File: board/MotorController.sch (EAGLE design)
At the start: 39 parts, among them IC1 ATMEGA328P-PU, Q1 BT137-600E, Q2 IPP80P03P4L-04, Q3 SUP75P03-07-H-NH, Y1 16Mhz

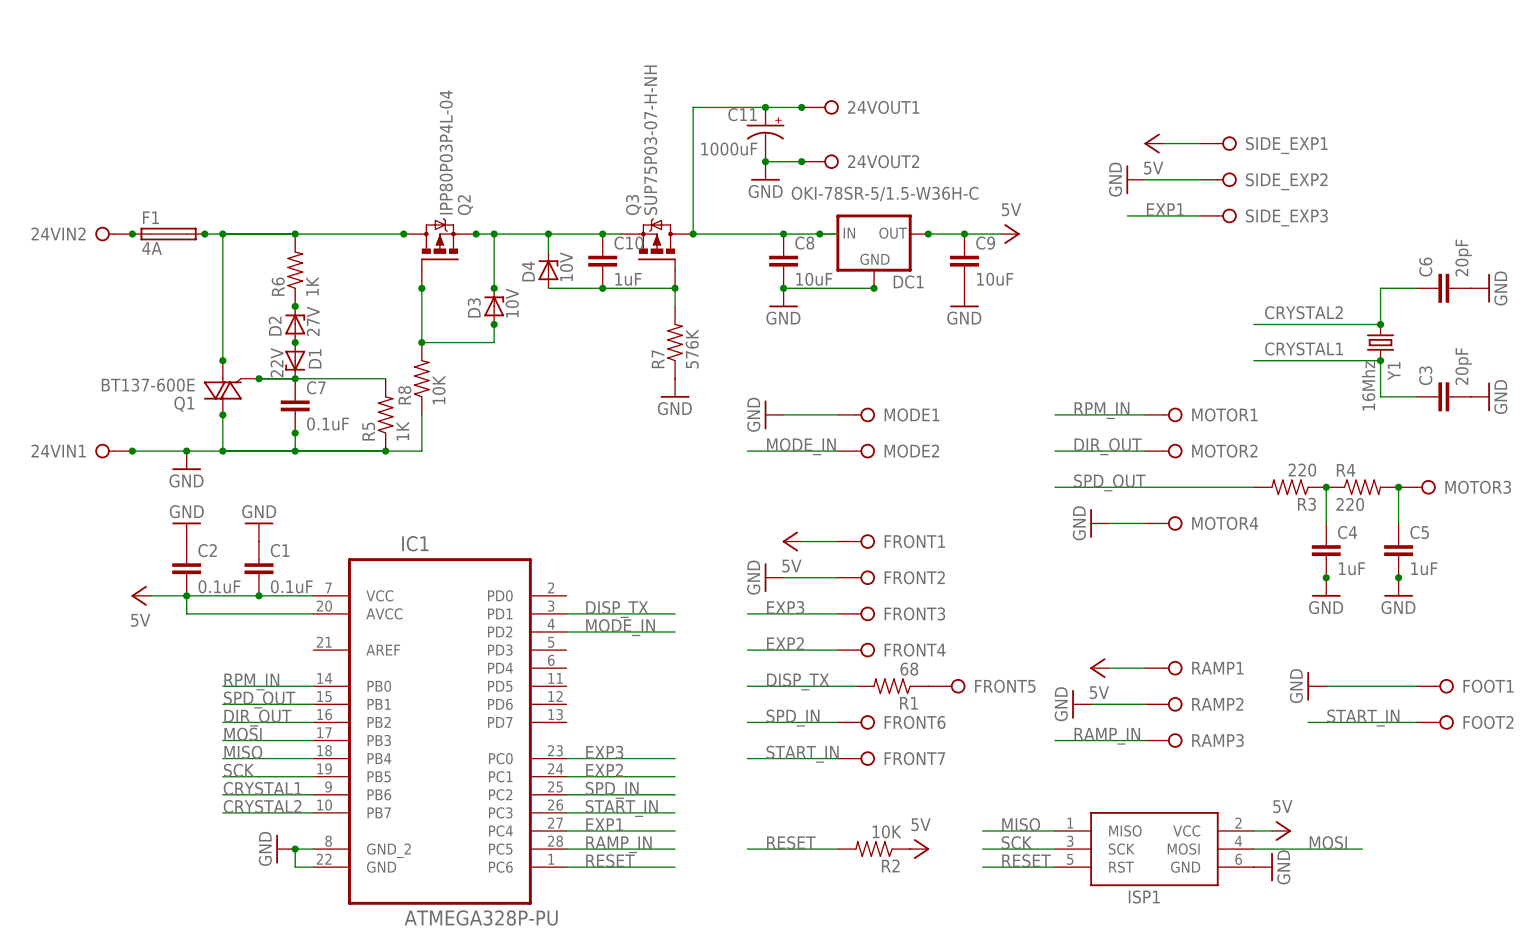
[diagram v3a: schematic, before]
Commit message: Fix the label order of caps
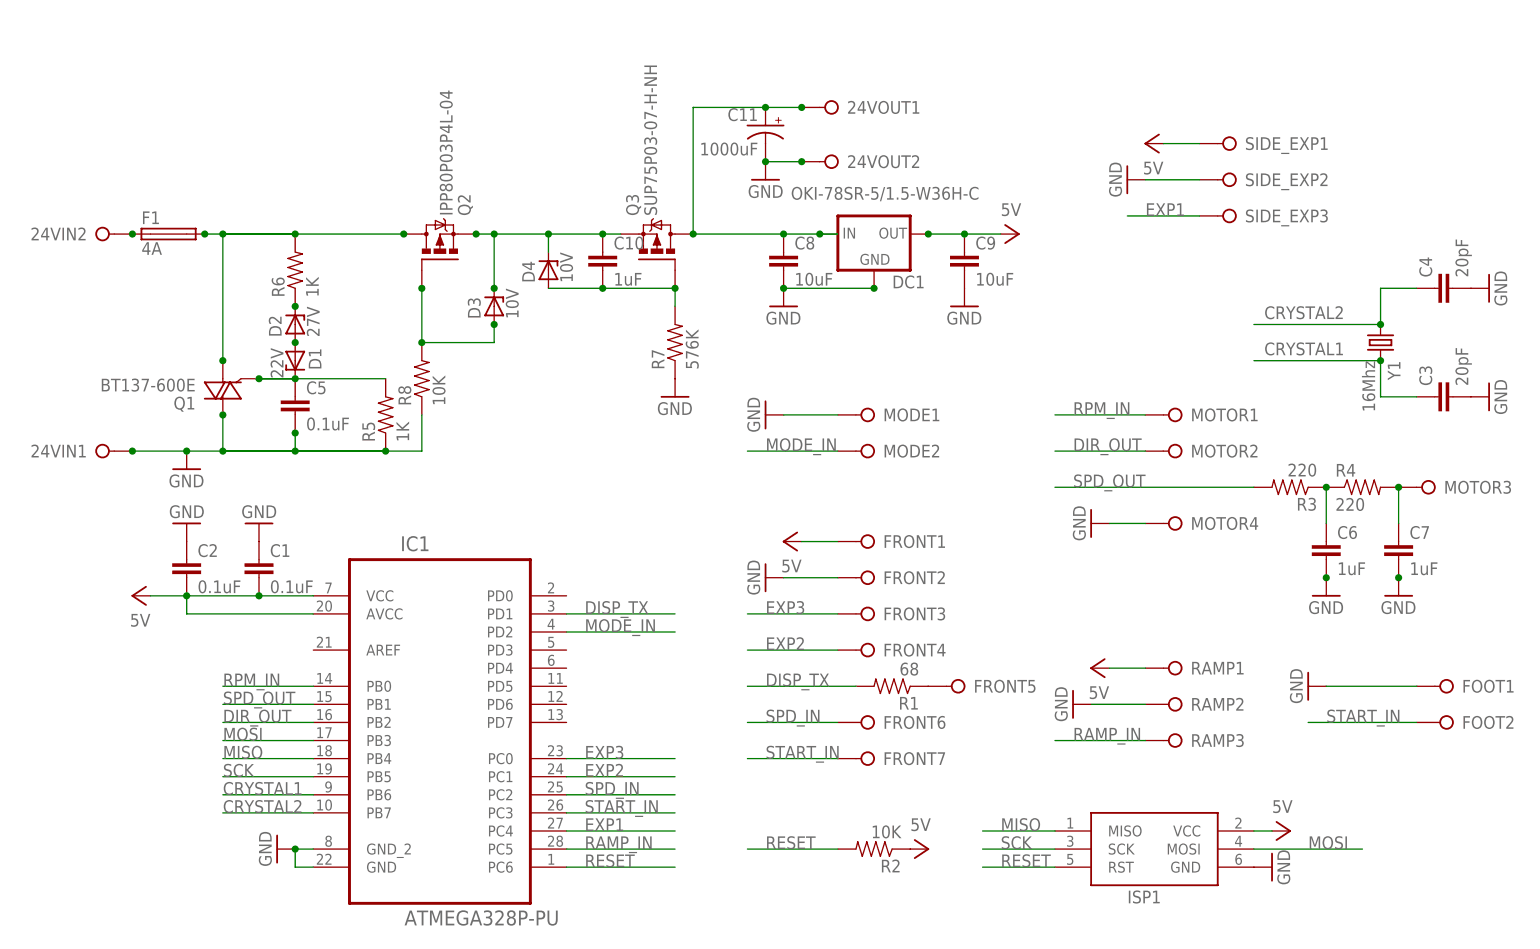
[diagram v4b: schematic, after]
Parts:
- C4: value 1uF -> 20pF
- C5: value 1uF -> 0.1uF
- C6: value 20pF -> 1uF
- C7: value 0.1uF -> 1uF
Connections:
- net CRYSTAL2: now also C4.1; no longer C6.1
- net N$1: now also C6.1; no longer C4.1
- net N$10: now also C7.1; no longer C5.1
- net N$7: now also C5.1; no longer C7.1
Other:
- moved on the sheet: C4, C5, C6, C7
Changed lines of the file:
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@@
 <part name="D2" library="SaintGimp" deviceset="ZENER" device="-7.5" value="27V"/>
 <part name="R6" library="SaintGimp" deviceset="RESISTOR-*" device="7.5MM" value="1K"/>
-<part name="C7" library="SaintGimp" deviceset="CAPACITOR-*" device="2.5MM" value="0.1uF"/>
+<part name="C5" library="SaintGimp" deviceset="CAPACITOR-*" device="2.5MM" value="0.1uF"/>
 <part name="R5" library="SaintGimp" deviceset="RESISTOR-*" device="7.5MM" value="1K"/>
 <part name="Q2" library="SaintGimp" deviceset="IPP80P03P4L-04" device="-H-NH" value="IPP80P03P4L-04"/>
@@
 <part name="R3" library="SaintGimp" deviceset="RESISTOR-*" device="7.5MM" value="220"/>
 <part name="R4" library="SaintGimp" deviceset="RESISTOR-*" device="7.5MM" value="220"/>
-<part name="C4" library="SaintGimp" deviceset="CAPACITOR-*" device="2.5MM" value="1uF"/>
+<part name="C6" library="SaintGimp" deviceset="CAPACITOR-*" device="2.5MM" value="1uF"/>
 <part name="GND7" library="SaintGimp" deviceset="GND" device=""/>
-<part name="C5" library="SaintGimp" deviceset="CAPACITOR-*" device="2.5MM" value="1uF"/>
+<part name="C7" library="SaintGimp" deviceset="CAPACITOR-*" device="2.5MM" value="1uF"/>
 <part name="GND8" library="SaintGimp" deviceset="GND" device=""/>
 <part name="Y1" library="SaintGimp" deviceset="CRYSTAL" device="-V" value="16Mhz"/>
 <part name="GND10" library="SaintGimp" deviceset="GND" device=""/>
 <part name="C3" library="SaintGimp" deviceset="CAPACITOR-*" device="2.5MM" value="20pF"/>
-<part name="C6" library="SaintGimp" deviceset="CAPACITOR-*" device="2.5MM" value="20pF"/>
+<part name="C4" library="SaintGimp" deviceset="CAPACITOR-*" device="2.5MM" value="20pF"/>
 <part name="GND11" library="SaintGimp" deviceset="GND" device=""/>
 <part name="GND12" library="SaintGimp" deviceset="GND" device=""/>
@@
 <instance part="D2" gate="G$1" x="-25.4" y="40.64" rot="R90"/>
 <instance part="R6" gate="G$1" x="-25.4" y="48.26" rot="R90"/>
-<instance part="C7" gate="G$1" x="-25.4" y="27.94"/>
+<instance part="C5" gate="G$1" x="-25.4" y="27.94"/>
 <instance part="R5" gate="G$1" x="-12.7" y="27.94" rot="R90"/>
 <instance part="Q2" gate="G$1" x="-5.08" y="50.8" rot="MR90"/>
@@
 <instance part="R3" gate="G$1" x="114.3" y="17.78" rot="R180"/>
 <instance part="R4" gate="G$1" x="124.46" y="17.78"/>
-<instance part="C4" gate="G$1" x="119.38" y="7.62"/>
+<instance part="C6" gate="G$1" x="119.38" y="7.62"/>
 <instance part="GND7" gate="1" x="119.38" y="2.54"/>
-<instance part="C5" gate="G$1" x="129.54" y="7.62"/>
+<instance part="C7" gate="G$1" x="129.54" y="7.62"/>
 <instance part="GND8" gate="1" x="129.54" y="2.54"/>
 <instance part="Y1" gate="G$1" x="127" y="38.1" rot="R270"/>
 <instance part="GND10" gate="1" x="-30.48" y="12.7" rot="R180"/>
 <instance part="C3" gate="G$1" x="137.16" y="30.48" rot="R90"/>
-<instance part="C6" gate="G$1" x="137.16" y="45.72" rot="R90"/>
+<instance part="C4" gate="G$1" x="137.16" y="45.72" rot="R90"/>
 <instance part="GND11" gate="1" x="142.24" y="30.48" rot="R90"/>
 <instance part="GND12" gate="1" x="142.24" y="45.72" rot="R90"/>
@@
 <wire x1="-12.7" y1="22.86" x2="-25.4" y2="22.86" width="0.1524" layer="91"/>
 <junction x="-12.7" y="22.86"/>
-<pinref part="C7" gate="G$1" pin="2"/>
+<pinref part="C5" gate="G$1" pin="2"/>
 <wire x1="-25.4" y1="22.86" x2="-35.56" y2="22.86" width="0.1524" layer="91"/>
 <wire x1="-35.56" y1="22.86" x2="-40.64" y2="22.86" width="0.1524" layer="91"/>
@@
 </segment>
 <segment>
-<pinref part="C5" gate="G$1" pin="2"/>
+<pinref part="C7" gate="G$1" pin="2"/>
 <pinref part="GND8" gate="1" pin="GND"/>
 <junction x="129.54" y="5.08"/>
@@
 </segment>
 <segment>
+<pinref part="C4" gate="G$1" pin="2"/>
+<pinref part="GND12" gate="1" pin="GND"/>
+</segment>
+<segment>
 <pinref part="C6" gate="G$1" pin="2"/>
-<pinref part="GND12" gate="1" pin="GND"/>
-</segment>
-<segment>
-<pinref part="C4" gate="G$1" pin="2"/>
-<pinref part="C4" gate="G$1" pin="2"/>
+<pinref part="C6" gate="G$1" pin="2"/>
 <pinref part="GND7" gate="1" pin="GND"/>
 <junction x="119.38" y="5.08"/>
@@
 <pinref part="D1" gate="G$1" pin="C"/>
 <wire x1="-30.48" y1="33.02" x2="-25.4" y2="33.02" width="0.1524" layer="91"/>
-<pinref part="C7" gate="G$1" pin="1"/>
+<pinref part="C5" gate="G$1" pin="1"/>
 <junction x="-25.4" y="33.02"/>
 <pinref part="R5" gate="G$1" pin="2"/>
@@
 <segment>
 <pinref part="R4" gate="G$1" pin="2"/>
-<pinref part="C5" gate="G$1" pin="1"/>
+<pinref part="C7" gate="G$1" pin="1"/>
 <wire x1="129.54" y1="12.7" x2="129.54" y2="17.78" width="0.1524" layer="91"/>
 <pinref part="MOTOR" gate="3" pin="KL"/>
@@
 <segment>
 <pinref part="Y1" gate="G$1" pin="1"/>
-<pinref part="C6" gate="G$1" pin="1"/>
+<pinref part="C4" gate="G$1" pin="1"/>
 <wire x1="132.08" y1="45.72" x2="127" y2="45.72" width="0.1524" layer="91"/>
 <wire x1="127" y1="45.72" x2="127" y2="40.64" width="0.1524" layer="91"/>
@@
 <pinref part="R3" gate="G$1" pin="1"/>
 <pinref part="R4" gate="G$1" pin="1"/>
-<pinref part="C4" gate="G$1" pin="1"/>
+<pinref part="C6" gate="G$1" pin="1"/>
 <wire x1="119.38" y1="12.7" x2="119.38" y2="17.78" width="0.1524" layer="91"/>
 <junction x="119.38" y="17.78"/>

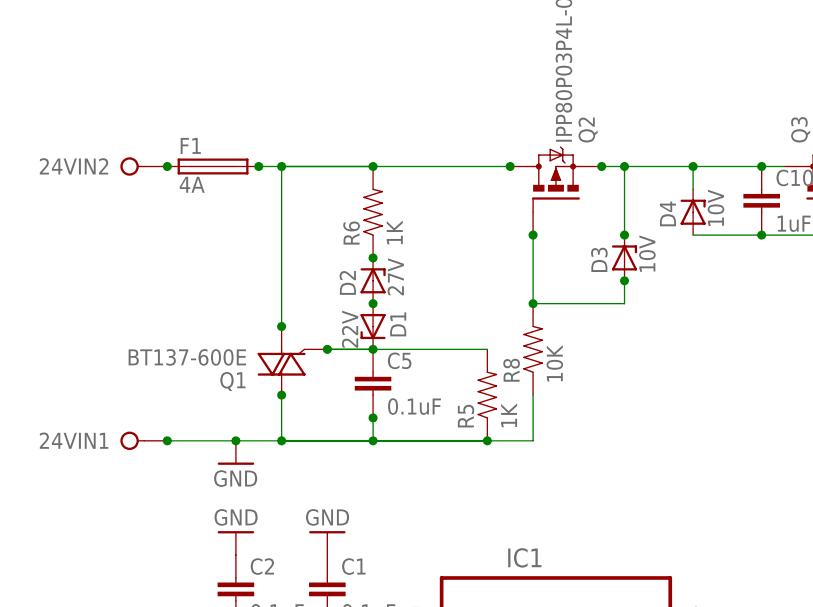
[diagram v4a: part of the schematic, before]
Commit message: Revert back to previous triac circuit
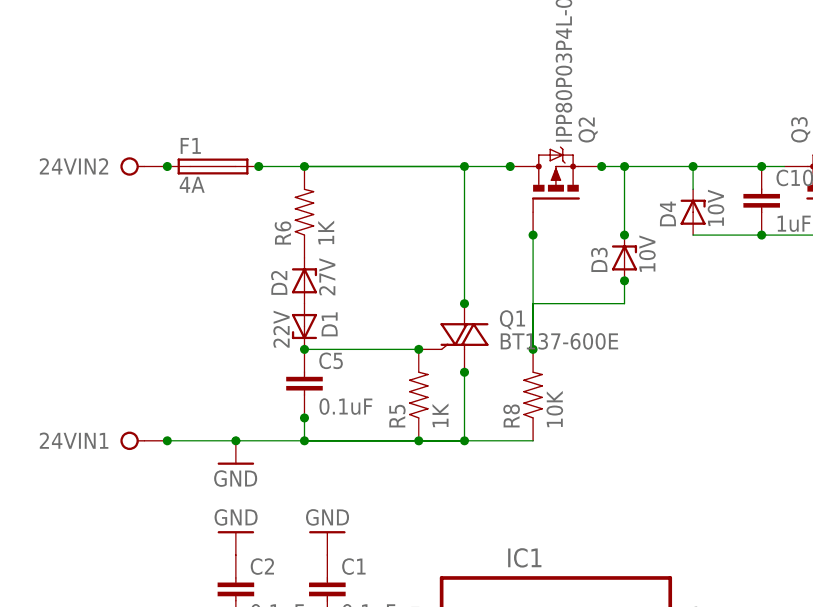
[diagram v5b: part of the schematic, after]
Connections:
- net 24V: now also Q1.A2; no longer Q1.A1
- net GND: now also Q1.A1; no longer Q1.A2
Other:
- moved on the sheet: C5, D1, D2, Q1, R5, R6, R8
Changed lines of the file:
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@@
 <instance part="C11" gate="G$1" x="40.64" y="68.58" rot="MR0"/>
 <instance part="F1" gate="G$1" x="-43.18" y="53.34"/>
-<instance part="Q1" gate="G$1" x="-35.56" y="33.02" rot="R180"/>
-<instance part="D1" gate="G$1" x="-25.4" y="35.56" rot="R270"/>
-<instance part="D2" gate="G$1" x="-25.4" y="40.64" rot="R90"/>
-<instance part="R6" gate="G$1" x="-25.4" y="48.26" rot="R90"/>
-<instance part="C5" gate="G$1" x="-25.4" y="27.94"/>
-<instance part="R5" gate="G$1" x="-12.7" y="27.94" rot="R90"/>
+<instance part="Q1" gate="G$1" x="-15.24" y="33.02"/>
+<instance part="D1" gate="G$1" x="-33.02" y="35.56" rot="R270"/>
+<instance part="D2" gate="G$1" x="-33.02" y="40.64" rot="R90"/>
+<instance part="R6" gate="G$1" x="-33.02" y="48.26" rot="R90"/>
+<instance part="C5" gate="G$1" x="-33.02" y="27.94"/>
+<instance part="R5" gate="G$1" x="-20.32" y="27.94" rot="R90"/>
 <instance part="Q2" gate="G$1" x="-5.08" y="50.8" rot="MR90"/>
-<instance part="R8" gate="G$1" x="-7.62" y="33.02" rot="R90"/>
+<instance part="R8" gate="G$1" x="-7.62" y="27.94" rot="R90"/>
 <instance part="D3" gate="G$1" x="2.54" y="43.18" rot="R90"/>
 <instance part="C9" gate="G$1" x="68.58" y="48.26"/>
@@
 </segment>
 <segment>
-<pinref part="Q1" gate="G$1" pin="A2"/>
-<wire x1="-35.56" y1="27.94" x2="-35.56" y2="22.86" width="0.1524" layer="91"/>
+<pinref part="Q1" gate="G$1" pin="A1"/>
+<wire x1="-15.24" y1="30.48" x2="-15.24" y2="22.86" width="0.1524" layer="91"/>
 <pinref part="R5" gate="G$1" pin="1"/>
-<wire x1="-35.56" y1="22.86" x2="-12.7" y2="22.86" width="0.1524" layer="91"/>
-<wire x1="-12.7" y1="22.86" x2="-25.4" y2="22.86" width="0.1524" layer="91"/>
-<junction x="-12.7" y="22.86"/>
+<wire x1="-20.32" y1="22.86" x2="-15.24" y2="22.86" width="0.1524" layer="91"/>
+<junction x="-20.32" y="22.86"/>
 <pinref part="C5" gate="G$1" pin="2"/>
-<wire x1="-25.4" y1="22.86" x2="-35.56" y2="22.86" width="0.1524" layer="91"/>
-<wire x1="-35.56" y1="22.86" x2="-40.64" y2="22.86" width="0.1524" layer="91"/>
+<wire x1="-33.02" y1="22.86" x2="-15.24" y2="22.86" width="0.1524" layer="91"/>
+<wire x1="-15.24" y1="22.86" x2="-40.64" y2="22.86" width="0.1524" layer="91"/>
 <wire x1="-40.64" y1="22.86" x2="-48.26" y2="22.86" width="0.1524" layer="91"/>
-<wire x1="-25.4" y1="25.4" x2="-25.4" y2="22.86" width="0.1524" layer="91"/>
-<junction x="-25.4" y="22.86"/>
+<wire x1="-33.02" y1="25.4" x2="-33.02" y2="22.86" width="0.1524" layer="91"/>
+<junction x="-33.02" y="22.86"/>
 <pinref part="R8" gate="G$1" pin="1"/>
-<wire x1="-7.62" y1="27.94" x2="-7.62" y2="22.86" width="0.1524" layer="91"/>
-<wire x1="-7.62" y1="22.86" x2="-35.56" y2="22.86" width="0.1524" layer="91"/>
-<junction x="-35.56" y="22.86"/>
+<wire x1="-7.62" y1="22.86" x2="-15.24" y2="22.86" width="0.1524" layer="91"/>
+<junction x="-15.24" y="22.86"/>
 <pinref part="24VIN" gate="1" pin="KL"/>
-<junction x="-35.56" y="27.94"/>
+<junction x="-15.24" y="30.48"/>
 <pinref part="GND4" gate="1" pin="GND"/>
 <junction x="-40.64" y="22.86"/>
 <junction x="-48.26" y="22.86"/>
-<junction x="-25.4" y="25.4"/>
+<junction x="-33.02" y="25.4"/>
 </segment>
 <segment>
@@
 <pinref part="R6" gate="G$1" pin="1"/>
 <pinref part="D2" gate="G$1" pin="C"/>
-<junction x="-25.4" y="43.18"/>
 </segment>
 </net>
@@
 <pinref part="D2" gate="G$1" pin="A"/>
 <pinref part="D1" gate="G$1" pin="A"/>
-<junction x="-25.4" y="38.1"/>
 </segment>
 </net>
@@
 <pinref part="Q1" gate="G$1" pin="G"/>
 <pinref part="D1" gate="G$1" pin="C"/>
-<wire x1="-30.48" y1="33.02" x2="-25.4" y2="33.02" width="0.1524" layer="91"/>
+<wire x1="-20.32" y1="33.02" x2="-33.02" y2="33.02" width="0.1524" layer="91"/>
 <pinref part="C5" gate="G$1" pin="1"/>
-<junction x="-25.4" y="33.02"/>
+<junction x="-33.02" y="33.02"/>
 <pinref part="R5" gate="G$1" pin="2"/>
-<junction x="-30.48" y="33.02"/>
-<wire x1="-30.48" y1="33.02" x2="-12.7" y2="33.02" width="0.1524" layer="91"/>
+<junction x="-20.32" y="33.02"/>
 </segment>
 </net>
@@
 <pinref part="F1" gate="G$1" pin="2"/>
 <pinref part="R6" gate="G$1" pin="2"/>
-<junction x="-25.4" y="53.34"/>
-<wire x1="-35.56" y1="53.34" x2="-38.1" y2="53.34" width="0.1524" layer="91"/>
-<wire x1="-25.4" y1="53.34" x2="-35.56" y2="53.34" width="0.1524" layer="91"/>
-<pinref part="Q1" gate="G$1" pin="A1"/>
-<wire x1="-35.56" y1="35.56" x2="-35.56" y2="53.34" width="0.1524" layer="91"/>
+<junction x="-33.02" y="53.34"/>
+<wire x1="-15.24" y1="53.34" x2="-38.1" y2="53.34" width="0.1524" layer="91"/>
+<wire x1="-33.02" y1="53.34" x2="-15.24" y2="53.34" width="0.1524" layer="91"/>
+<pinref part="Q1" gate="G$1" pin="A2"/>
+<wire x1="-15.24" y1="38.1" x2="-15.24" y2="53.34" width="0.1524" layer="91"/>
 <pinref part="Q2" gate="G$1" pin="D"/>
-<wire x1="-10.16" y1="53.34" x2="-35.56" y2="53.34" width="0.1524" layer="91"/>
-<junction x="-35.56" y="53.34"/>
+<wire x1="-10.16" y1="53.34" x2="-15.24" y2="53.34" width="0.1524" layer="91"/>
+<junction x="-15.24" y="53.34"/>
 <junction x="-10.16" y="53.34"/>
-<junction x="-35.56" y="35.56"/>
+<junction x="-15.24" y="38.1"/>
 <junction x="-38.1" y="53.34"/>
 </segment>
@@
 <pinref part="Q2" gate="G$1" pin="G"/>
 <pinref part="R8" gate="G$1" pin="2"/>
-<wire x1="-7.62" y1="45.72" x2="-7.62" y2="38.1" width="0.1524" layer="91"/>
+<wire x1="-7.62" y1="45.72" x2="-7.62" y2="33.02" width="0.1524" layer="91"/>
 <pinref part="D3" gate="G$1" pin="A"/>
 <wire x1="2.54" y1="40.64" x2="2.54" y2="38.1" width="0.1524" layer="91"/>
 <wire x1="2.54" y1="38.1" x2="-7.62" y2="38.1" width="0.1524" layer="91"/>
-<junction x="-7.62" y="38.1"/>
+<wire x1="-7.62" y1="38.1" x2="-7.62" y2="33.02" width="0.1524" layer="91"/>
+<junction x="-7.62" y="33.02"/>
 <junction x="-7.62" y="45.72"/>
 <junction x="2.54" y="40.64"/>
